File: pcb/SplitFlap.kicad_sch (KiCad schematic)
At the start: 22 parts, among them J1 A1_3, U1 PCF8575DBR, U2 ULN2003

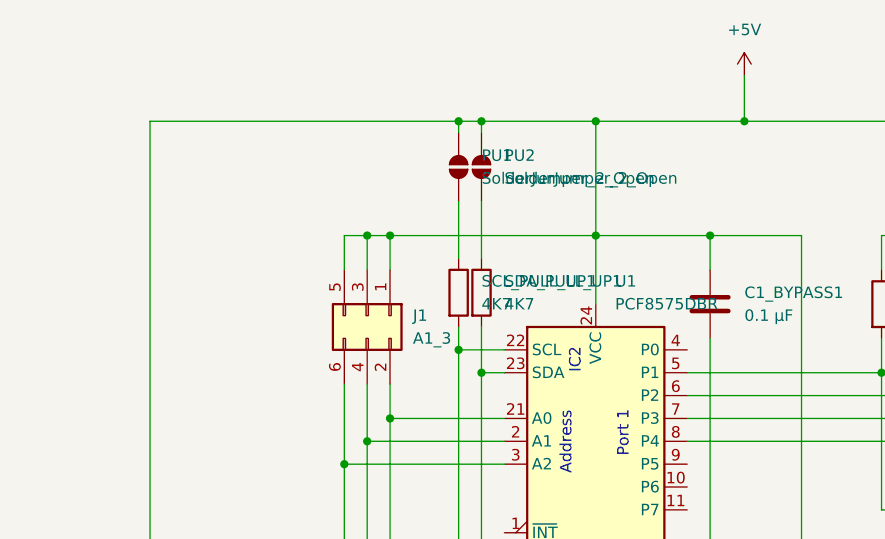
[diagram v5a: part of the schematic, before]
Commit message: Remove pull-ups entirely
For now manually soldering pull-ups to the ESP32 remain an easier solution.
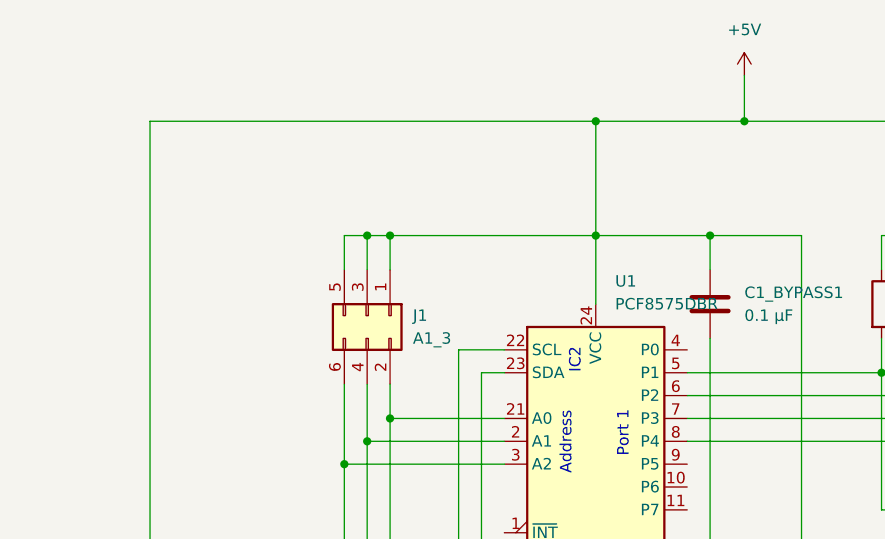
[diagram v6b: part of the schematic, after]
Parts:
- removed PU1, PU2: SolderJumper_2_Open, Jumper:SolderJumper-2_P1.3mm_Open_RoundedPad1.0x1.5mm, symbol Jumper:SolderJumper_2_Open
- removed SCL_PULL_UP1, SDA_PULL_UP1: 4K7, Resistor_SMD:R_0603_1608Metric, symbol Device:R
